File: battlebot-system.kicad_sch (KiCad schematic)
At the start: 1 part

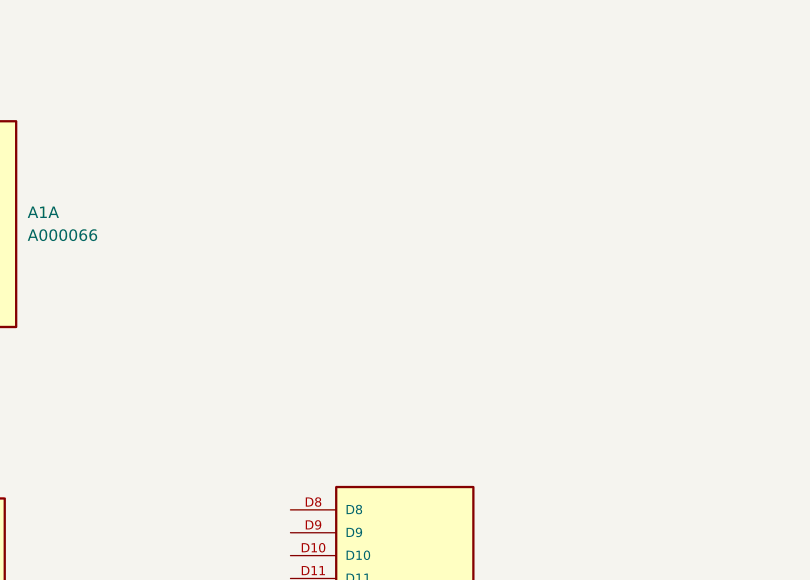
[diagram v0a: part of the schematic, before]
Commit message: Add and update datasheets to match symbols
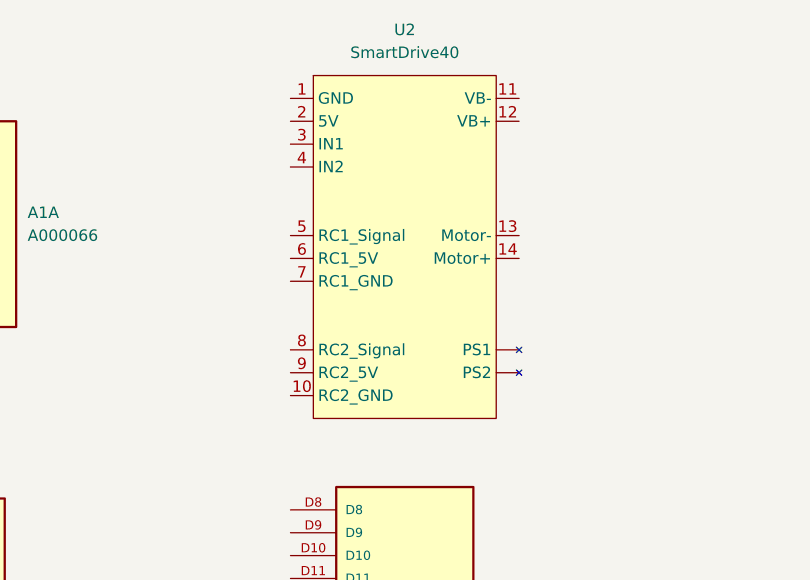
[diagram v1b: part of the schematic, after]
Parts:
- added U2: SmartDrive40, symbol battlebot_library:MDS40B
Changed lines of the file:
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@@
 			)
 		)
-		(property "Datasheet" ""
-			(at 31.75 41.91 0)
-			(effects
-				(font
-					(size 1.27 1.27)
-				)
-				(hide yes)
-			)
-		)
-		(property "Description" ""
+		(property "Datasheet" "kicad-embed://A000066_Arduino.pdf"
+			(at 31.75 41.91 0)
+			(effects
+				(font
+					(size 1.27 1.27)
+				)
+				(hide yes)
+			)
+		)
+		(property "Description" "Arduino UNO Rev3 Microcontroller Board, ATmega328P | Arduino A000066"
 			(at 31.75 41.91 0)
 			(effects
@@
 			)
 		)
-		(property "Datasheet" ""
-			(at 82.55 82.55 0)
-			(effects
-				(font
-					(size 1.27 1.27)
-				)
-				(hide yes)
-			)
-		)
-		(property "Description" ""
+		(property "Datasheet" "kicad-embed://A000066_Arduino.pdf"
+			(at 82.55 82.55 0)
+			(effects
+				(font
+					(size 1.27 1.27)
+				)
+				(hide yes)
+			)
+		)
+		(property "Description" "Arduino UNO Rev3 Microcontroller Board, ATmega328P | Arduino A000066"
 			(at 82.55 82.55 0)
 			(effects
@@
 			)
 		)
-		(property "Datasheet" ""
-			(at 30.48 81.28 0)
-			(effects
-				(font
-					(size 1.27 1.27)
-				)
-				(hide yes)
-			)
-		)
-		(property "Description" ""
+		(property "Datasheet" "kicad-embed://A000066_Arduino.pdf"
+			(at 30.48 81.28 0)
+			(effects
+				(font
+					(size 1.27 1.27)
+				)
+				(hide yes)
+			)
+		)
+		(property "Description" "Arduino UNO Rev3 Microcontroller Board, ATmega328P | Arduino A000066"
 			(at 30.48 81.28 0)
 			(effects
@@
 				)
 			)
+		)
+	)
+	(symbol
+		(lib_id "battlebot_library:MDS40B")
+		(at 76.2 33.02 0)
+		(unit 1)
+		(exclude_from_sim no)
+		(in_bom yes)
+		(on_board yes)
+		(dnp no)
+		(fields_autoplaced yes)
+		(property "Reference" "U2"
+			(at 82.55 19.05 0)
+			(effects
+				(font
+					(size 1.27 1.27)
+				)
+			)
+		)
+		(property "Value" "SmartDrive40"
+			(at 82.55 21.59 0)
+			(effects
+				(font
+					(size 1.27 1.27)
+				)
+			)
+		)
+		(property "Footprint" ""
+			(at 76.2 33.02 0)
+			(effects
+				(font
+					(size 1.27 1.27)
+				)
+				(hide yes)
+			)
+		)
+		(property "Datasheet" ""
+			(at 76.2 33.02 0)
+			(effects
+				(font
+					(size 1.27 1.27)
+				)
+				(hide yes)
+			)
+		)
+		(property "Description" ""
+			(at 76.2 33.02 0)
+			(effects
+				(font
+					(size 1.27 1.27)
+				)
+				(hide yes)
+			)
+		)
+		(pin ""
+		)
+		(pin ""
+		)
+		(pin "13"
+		)
+		(pin "12"
+		)
+		(pin "11"
+		)
+		(pin "10"
+		)
+		(pin "9"
+		)
+		(pin "8"
+		)
+		(pin "7"
+		)
+		(pin "6"
+		)
+		(pin "5"
+		)
+		(pin "4"
+		)
+		(pin "3"
+		)
+		(pin "2"
+		)
+		(pin "1"
+		)
+		(pin "14"
+		)
+		(instances
+			(project ""
+				(path "/a350ff7a-a547-44b8-aa5d-3d9eed7f09e0"
+					(reference "U2")
+					(unit 1)
+				)
+			)
